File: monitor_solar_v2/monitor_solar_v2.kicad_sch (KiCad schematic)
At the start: 25 parts, among them J1 Screw_Terminal_01x02, J2 Conn_01x03_Socket, J3 Screw_Terminal_01x02, J4 Conn_01x04_Pin, J5 Conn_01x03_Pin, U1 X9C103S, U2 AMS1117-3.3, U4 LM358

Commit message: feat: v2 pcb con board potenciometro a medida
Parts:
- U1: footprint SOIC8_3P9116X4P9022_INR -> RF_GPS:X9C103S
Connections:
- net +5V: now also J3.1 (Pin_1); no longer J3.2 (Pin_2)
- net GND: now also J3.2 (Pin_2); no longer J3.1 (Pin_1)
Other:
- moved on the sheet: C1, C2, C4, C5, D1, D2, H1, H2, H3, H4, J1, J2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

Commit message: Cambios menores
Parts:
- added U3: ESP-12E, RF_Module:ESP-12E, symbol RF_Module:ESP-12E
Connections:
- net +3.3V: now also J4.4 (Pin_4), U3.8 (VCC); no longer J4.1 (Pin_1)
- net GND: now also J4.1 (Pin_1), U3.15 (GND); no longer J4.4 (Pin_4)
- net Vamp1: now also C2.1, D2.2 (A), J4.3 (Pin_3), R4.2; no longer R4.1, U4.1, U4.2 (-)
- net Vamp2: now reaches C1.1, D1.2 (A), J4.2 (Pin_2), R3.2
- new net: R4.1, U4.1, U4.2 (-)
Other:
- moved on the sheet: C1, C2, D1, D2, J5, R3, R4, U1

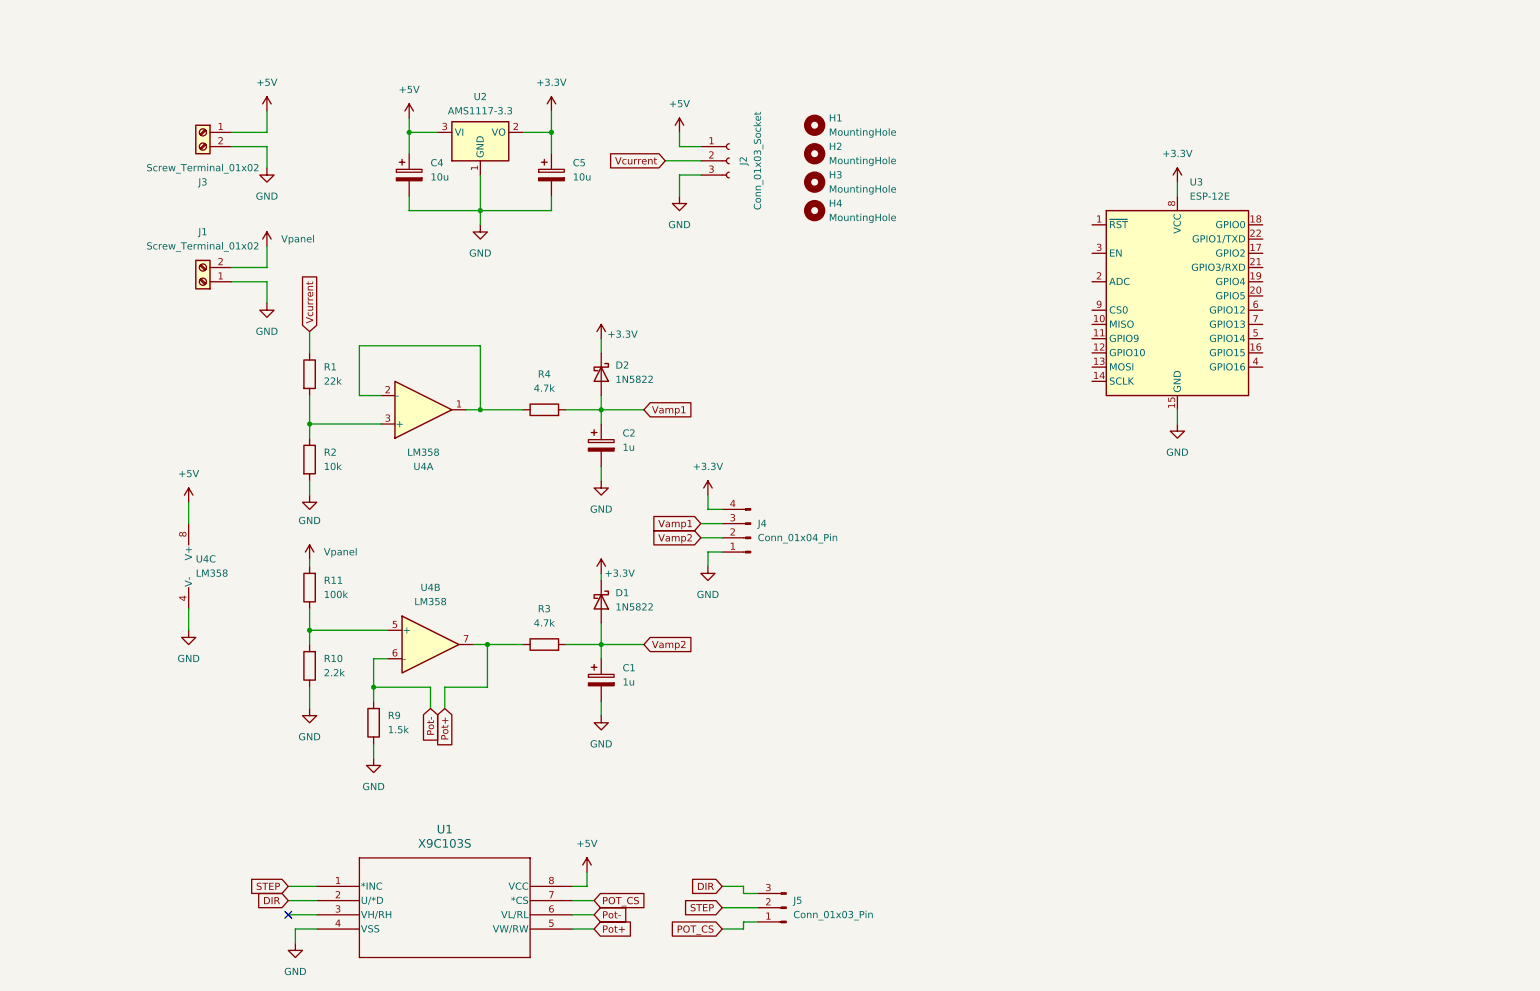
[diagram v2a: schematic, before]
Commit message: Adding ESP-12 and new pcb
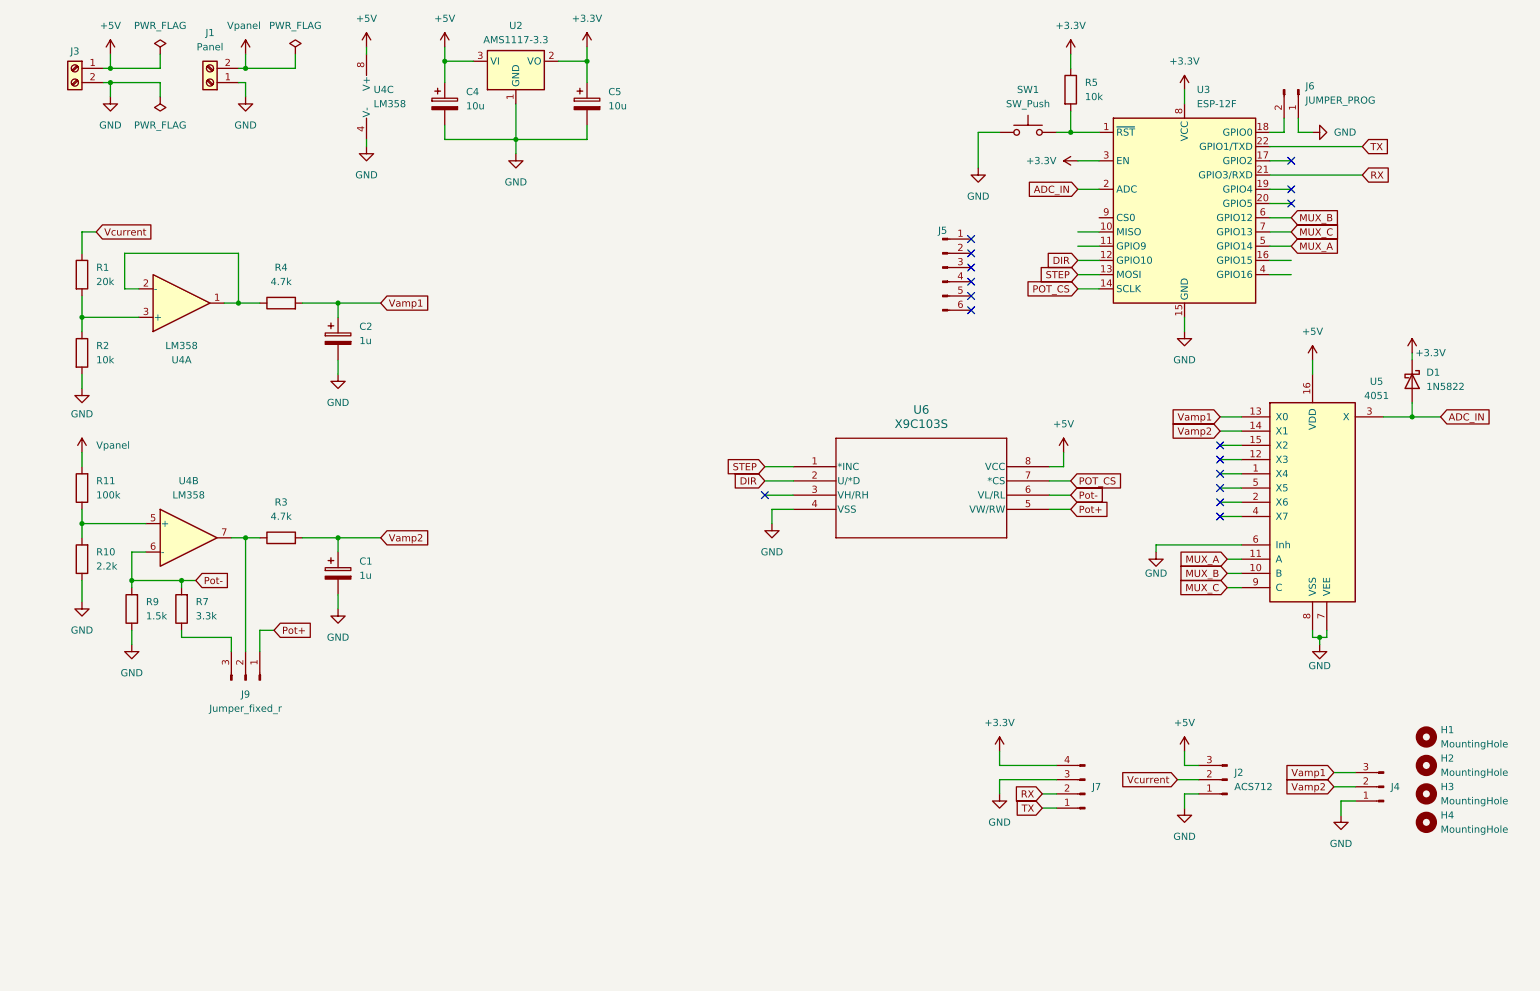
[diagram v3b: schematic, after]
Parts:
- removed D2: 1N5822, Diode_THT:D_DO-201AD_P15.24mm_Horizontal, symbol Diode:1N5822
- removed J2: Conn_01x03_Socket, Connector_PinHeader_2.54mm:PinHeader_1x03_P2.54mm_Vertical, symbol Connector:Conn_01x03_Socket
- removed J4: Conn_01x04_Pin, Connector_PinHeader_2.54mm:PinHeader_1x04_P2.54mm_Vertical, symbol Connector:Conn_01x04_Pin
- removed J5: Conn_01x03_Pin, Connector_PinHeader_2.54mm:PinHeader_1x03_P2.54mm_Vertical, symbol Connector:Conn_01x03_Pin
- removed U1: X9C103S, RF_GPS:X9C103S, symbol 2024-08-13_23-58-24:X9C103S
- removed U3: ESP-12E, RF_Module:ESP-12E, symbol RF_Module:ESP-12E
- added J2: ACS712, Connector_PinHeader_2.54mm:PinHeader_1x03_P2.54mm_Vertical, symbol Connector:Conn_01x03_Pin
- added J4: AMP_OUT, Connector_PinHeader_2.54mm:PinHeader_1x03_P2.54mm_Vertical, symbol Connector:Conn_01x03_Pin
- added J5: GPIO, Connector_PinHeader_2.54mm:PinHeader_1x06_P2.54mm_Vertical, symbol Connector:Conn_01x06_Pin
- added J6: JUMPER_PROG, Connector_PinHeader_2.54mm:PinHeader_1x02_P2.54mm_Vertical, symbol Connector:Conn_01x02_Pin
- added J7: PROGRAM, Connector_PinHeader_2.54mm:PinHeader_1x04_P2.54mm_Vertical, symbol Connector:Conn_01x04_Pin
- added J9: Jumper_fixed_r, Connector_PinHeader_2.54mm:PinHeader_1x03_P2.54mm_Vertical, symbol Connector:Conn_01x03_Pin
- added R5: 10k, Resistor_THT:R_Axial_DIN0207_L6.3mm_D2.5mm_P10.16mm_Horizontal, symbol Device:R
- added R7: 3.3k, Resistor_THT:R_Axial_DIN0207_L6.3mm_D2.5mm_P10.16mm_Horizontal, symbol Device:R
- added SW1: SW_Push, Button_Switch_THT:SW_PUSH_6mm, symbol Switch:SW_Push
- added U3: ESP-12F, RF_Module:ESP-12E, symbol RF_Module:ESP-12F
- added U5: 4051, Package_DIP:DIP-16_W7.62mm_Socket_LongPads, symbol 4xxx:4051
- added U6: X9C103S, Componentes:X9C103S, symbol x9c103s:X9C103S
- J1: value Screw_Terminal_01x02 -> Panel
- J3: value Screw_Terminal_01x02 -> Reg 5V
- R1: value 22k -> 20k
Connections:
- net +3.3V: now also J7.4 (Pin_4), R5.1, U3.3 (EN), U3.8 (VCC)
- net +5V: now also J2.3 (Pin_3), U5.16 (VDD), U6.8 (VCC)
- net DIR: now also U3.12 (GPIO10), U6.2 (U/*D)
- net GND: now also J2.1 (Pin_1), J4.1 (Pin_1), J6.1 (Pin_1), J7.3 (Pin_3), SW1.1, U3.15 (GND), U5.6 (Inh), U5.7 (VEE), U5.8 (VSS), U6.4 (VSS)
- net POT_CS: now also U3.14 (SCLK), U6.7 (*CS)
- net Pot+: now also J9.1 (Pin_1), U6.5 (VW/RW); no longer R3.1, U4.7
- net Pot-: now also R7.2, U6.6 (VL/RL)
- net STEP: now also U3.13 (MOSI), U6.1 (*INC)
- net Vamp1: now also J4.3 (Pin_3), U5.13 (X0)
- net Vamp2: now also J4.2 (Pin_2), U5.14 (X1); no longer D1.2 (A)
- net Vcurrent: now also J2.2 (Pin_2)
- new net: J9.2 (Pin_2), R3.1, U4.7
- new net: R5.2, SW1.2, U3.1 (~{RST})
- new net: J6.2 (Pin_2), U3.18 (GPIO0)
- new net: J9.3 (Pin_3), R7.1
- new net ADC_IN: D1.2 (A), U3.2 (ADC), U5.3 (X)
- new net MUX_A: U3.5 (GPIO14), U5.11 (A)
- new net MUX_B: U3.6 (GPIO12), U5.10 (B)
- new net MUX_C: U3.7 (GPIO13), U5.9 (C)
- new net RX: J7.2 (Pin_2), U3.21 (GPIO3/RXD)
- new net TX: J7.1 (Pin_1), U3.22 (GPIO1/TXD)
- no-connect marks 1 -> 16
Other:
- moved on the sheet: C1, C2, C4, C5, H1, H2, H3, H4, J1, J3, R1, R10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

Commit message: PCB esp12 v1.0
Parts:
- removed J5: GPIO, Connector_PinHeader_2.54mm:PinHeader_1x06_P2.54mm_Vertical, symbol Connector:Conn_01x06_Pin
- added J5: JUMPER_PROG, Connector_PinHeader_2.54mm:PinHeader_1x02_P2.54mm_Vertical, symbol Connector:Conn_01x02_Pin
- added J8: GPIO_2, Connector_PinHeader_2.54mm:PinHeader_1x02_P2.54mm_Vertical, symbol Connector:Conn_01x02_Pin
- added R6: 10k, Resistor_THT:R_Axial_DIN0207_L6.3mm_D2.5mm_P10.16mm_Horizontal, symbol Device:R
- J1: footprint TerminalBlock_Phoenix:TerminalBlock_Phoenix_MKDS-1,5-2_1x02_P5.00mm_Horizontal -> TerminalBlock_Phoenix:TerminalBlock_Phoenix_MKDS-1,5-2-5.08_1x02_P5.08mm_Horizontal
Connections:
- net +3.3V: now also U3.20 (GPIO5), U3.4 (GPIO16), R6.1; no longer U3.3 (EN)
- net DIR: now also U3.10 (MISO); no longer U3.12 (GPIO10)
- net GND: now also J4.2 (Pin_2), U3.9 (CS0); no longer J4.1 (Pin_1)
- net MUX_A: now also U3.7 (GPIO13); no longer U3.5 (GPIO14)
- net MUX_B: now also U3.5 (GPIO14); no longer U3.6 (GPIO12)
- net MUX_C: now also U3.6 (GPIO12); no longer U3.7 (GPIO13)
- net POT_CS: now also U3.12 (GPIO10); no longer U3.14 (SCLK)
- net STEP: now also U3.11 (GPIO9); no longer U3.13 (MOSI)
- net Vamp2: now also J4.1 (Pin_1); no longer J4.2 (Pin_2)
- net GPIO15: now reaches U3.16 (GPIO15)
- net GPIO15: now also J5.1 (Pin_1)
- net GPIO2: now reaches U3.17 (GPIO2)
- net GPIO2: now also J5.2 (Pin_2)
- new net: J8.1 (Pin_1), U3.13 (MOSI)
- new net: J8.2 (Pin_2), U3.14 (SCLK)
- new net: R6.2, U3.3 (EN)
- no-connect marks 16 -> 8
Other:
- moved on the sheet: R5, SW1

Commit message: codigo v1: pruebas en telegram
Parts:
- R1: value 20k -> 22k
- R2: value 10k -> 33k
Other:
- moved on the sheet: J2, J4, J5, U6
